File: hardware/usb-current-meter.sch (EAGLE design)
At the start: 30 parts, among them IC2 LM358, U1 ATTINY45, X1 MC2, X3 USB-A-H

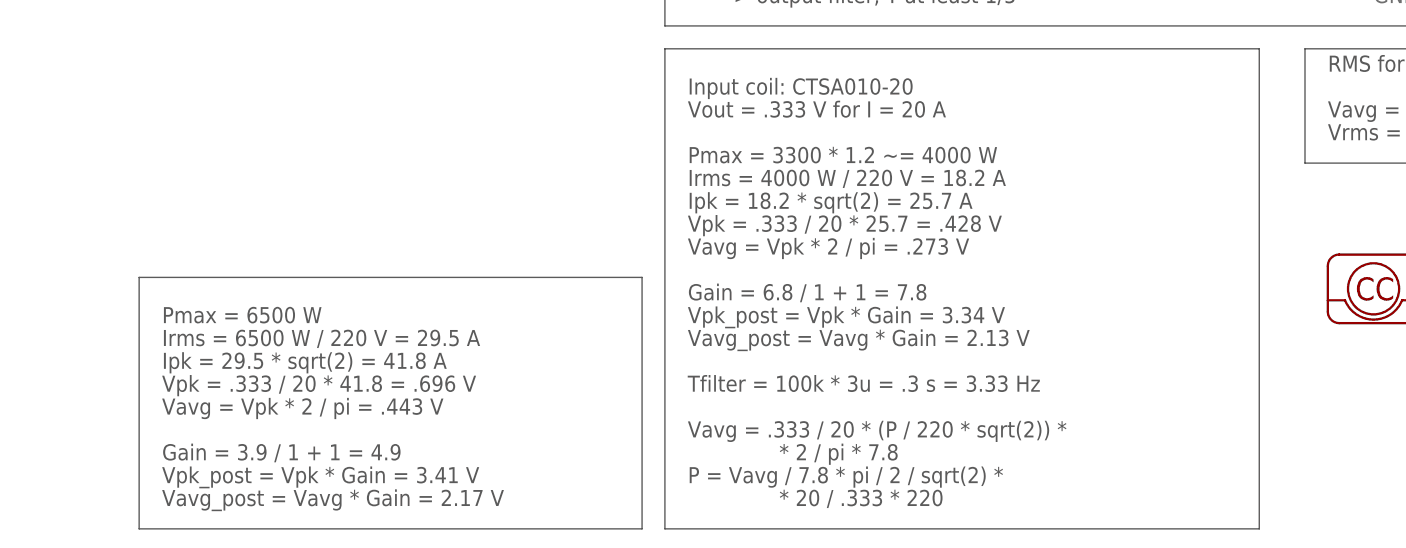
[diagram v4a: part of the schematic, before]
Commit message: hardware: re-made calculations for 230V (welcome to 2012)
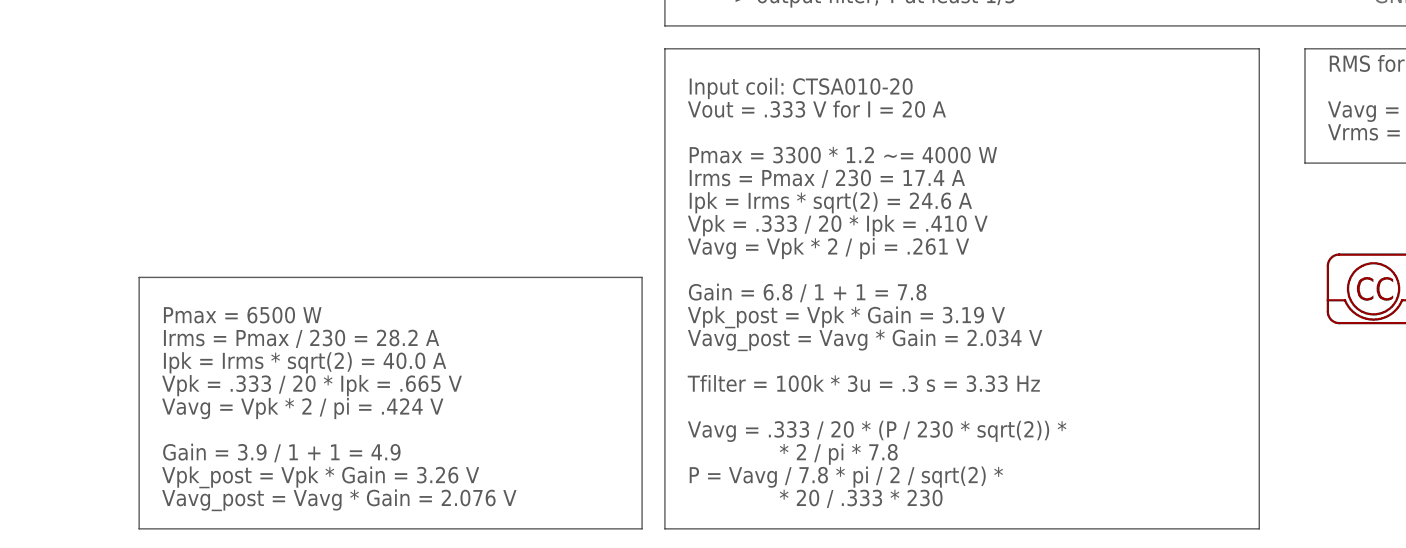
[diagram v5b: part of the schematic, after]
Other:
- note added: "* 20 / .333 * 230"
- note added: "Ipk = Irms * sqrt(2) = 24.6 A"
- note added: "Ipk = Irms * sqrt(2) = 40.0 A"
- note added: "Irms = Pmax / 230 = 17.4 A"
- note added: "Irms = Pmax / 230 = 28.2 A"
- note added: "Vavg = .333 / 20 * (P / 230 * sqrt(2)) *"
- note added: "Vavg = Vpk * 2 / pi = .261 V"
- note added: "Vavg = Vpk * 2 / pi = .424 V"
- note added: "Vavg_post = Vavg * Gain = 2.034 V"
- note added: "Vavg_post = Vavg * Gain = 2.076 V"
- note added: "Vpk = .333 / 20 * Ipk = .410 V"
- note added: "Vpk = .333 / 20 * Ipk = .665 V"
- note added: "Vpk_post = Vpk * Gain = 3.19 V"
- note added: "Vpk_post = Vpk * Gain = 3.26 V"
- note removed: "* 20 / .333 * 220"
- note removed: "Ipk = 18.2 * sqrt(2) = 25.7 A"
- note removed: "Ipk = 29.5 * sqrt(2) = 41.8 A"
- note removed: "Irms = 4000 W / 220 V = 18.2 A"
- note removed: "Irms = 6500 W / 220 V = 29.5 A"
- note removed: "Vavg = .333 / 20 * (P / 220 * sqrt(2)) *"
- note removed: "Vavg = Vpk * 2 / pi = .273 V"
- note removed: "Vavg = Vpk * 2 / pi = .443 V"
- note removed: "Vavg_post = Vavg * Gain = 2.13 V"
- note removed: "Vavg_post = Vavg * Gain = 2.17 V"
- note removed: "Vpk = .333 / 20 * 25.7 = .428 V"
- note removed: "Vpk = .333 / 20 * 41.8 = .696 V"
- note removed: "Vpk_post = Vpk * Gain = 3.34 V"
- note removed: "Vpk_post = Vpk * Gain = 3.41 V"
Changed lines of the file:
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@@
 <text x="99.06" y="60.96" size="1.778" layer="97">&gt; output filter, T at least 1/5</text>
 <text x="93.98" y="43.18" size="1.778" layer="97">Pmax = 3300 * 1.2 ~= 4000 W</text>
-<text x="93.98" y="40.64" size="1.778" layer="97">Irms = 4000 W / 220 V = 18.2 A</text>
-<text x="93.98" y="38.1" size="1.778" layer="97">Ipk = 18.2 * sqrt(2) = 25.7 A</text>
-<text x="93.98" y="35.56" size="1.778" layer="97">Vpk = .333 / 20 * 25.7 = .428 V</text>
+<text x="93.98" y="40.64" size="1.778" layer="97">Irms = Pmax / 230 = 17.4 A</text>
+<text x="93.98" y="38.1" size="1.778" layer="97">Ipk = Irms * sqrt(2) = 24.6 A</text>
+<text x="93.98" y="35.56" size="1.778" layer="97">Vpk = .333 / 20 * Ipk = .410 V</text>
 <text x="93.98" y="48.26" size="1.778" layer="97">Vout = .333 V for I = 20 A</text>
 <text x="93.98" y="50.8" size="1.778" layer="97">Input coil: CTSA010-20</text>
-<text x="93.98" y="33.02" size="1.778" layer="97">Vavg = Vpk * 2 / pi = .273 V</text>
+<text x="93.98" y="33.02" size="1.778" layer="97">Vavg = Vpk * 2 / pi = .261 V</text>
 <text x="93.98" y="27.94" size="1.778" layer="97">Gain = 6.8 / 1 + 1 = 7.8</text>
-<text x="93.98" y="25.4" size="1.778" layer="97">Vpk_post = Vpk * Gain = 3.34 V</text>
-<text x="93.98" y="22.86" size="1.778" layer="97">Vavg_post = Vavg * Gain = 2.13 V</text>
+<text x="93.98" y="25.4" size="1.778" layer="97">Vpk_post = Vpk * Gain = 3.19 V</text>
+<text x="93.98" y="22.86" size="1.778" layer="97">Vavg_post = Vavg * Gain = 2.034 V</text>
 <text x="165.1" y="53.34" size="1.778" layer="97">RMS for sine wave</text>
 <text x="165.1" y="48.26" size="1.778" layer="97">Vavg = Vpk * 2 / pi</text>
@@
 <wire x1="162.56" y1="43.18" x2="162.56" y2="55.88" width="0.1524" layer="97"/>
 <text x="93.98" y="17.78" size="1.778" layer="97">Tfilter = 100k * 3u = .3 s = 3.33 Hz</text>
-<text x="93.98" y="12.7" size="1.778" layer="97">Vavg = .333 / 20 * (P / 220 * sqrt(2)) *</text>
+<text x="93.98" y="12.7" size="1.778" layer="97">Vavg = .333 / 20 * (P / 230 * sqrt(2)) *</text>
 <text x="104.14" y="10.16" size="1.778" layer="97">* 2 / pi * 7.8</text>
 <text x="93.98" y="7.62" size="1.778" layer="97">P = Vavg / 7.8 * pi / 2 / sqrt(2) *</text>
-<text x="104.14" y="5.08" size="1.778" layer="97">* 20 / .333 * 220</text>
+<text x="104.14" y="5.08" size="1.778" layer="97">* 20 / .333 * 230</text>
 <text x="35.56" y="25.4" size="1.778" layer="97">Pmax = 6500 W</text>
-<text x="35.56" y="22.86" size="1.778" layer="97">Irms = 6500 W / 220 V = 29.5 A</text>
-<text x="35.56" y="20.32" size="1.778" layer="97">Ipk = 29.5 * sqrt(2) = 41.8 A</text>
-<text x="35.56" y="17.78" size="1.778" layer="97">Vpk = .333 / 20 * 41.8 = .696 V</text>
-<text x="35.56" y="15.24" size="1.778" layer="97">Vavg = Vpk * 2 / pi = .443 V</text>
+<text x="35.56" y="22.86" size="1.778" layer="97">Irms = Pmax / 230 = 28.2 A</text>
+<text x="35.56" y="20.32" size="1.778" layer="97">Ipk = Irms * sqrt(2) = 40.0 A</text>
+<text x="35.56" y="17.78" size="1.778" layer="97">Vpk = .333 / 20 * Ipk = .665 V</text>
+<text x="35.56" y="15.24" size="1.778" layer="97">Vavg = Vpk * 2 / pi = .424 V</text>
 <text x="35.56" y="10.16" size="1.778" layer="97">Gain = 3.9 / 1 + 1 = 4.9</text>
-<text x="35.56" y="7.62" size="1.778" layer="97">Vpk_post = Vpk * Gain = 3.41 V</text>
-<text x="35.56" y="5.08" size="1.778" layer="97">Vavg_post = Vavg * Gain = 2.17 V</text>
+<text x="35.56" y="7.62" size="1.778" layer="97">Vpk_post = Vpk * Gain = 3.26 V</text>
+<text x="35.56" y="5.08" size="1.778" layer="97">Vavg_post = Vavg * Gain = 2.076 V</text>
 <wire x1="33.02" y1="30.48" x2="88.9" y2="30.48" width="0.1524" layer="97"/>
 <wire x1="88.9" y1="30.48" x2="88.9" y2="2.54" width="0.1524" layer="97"/>

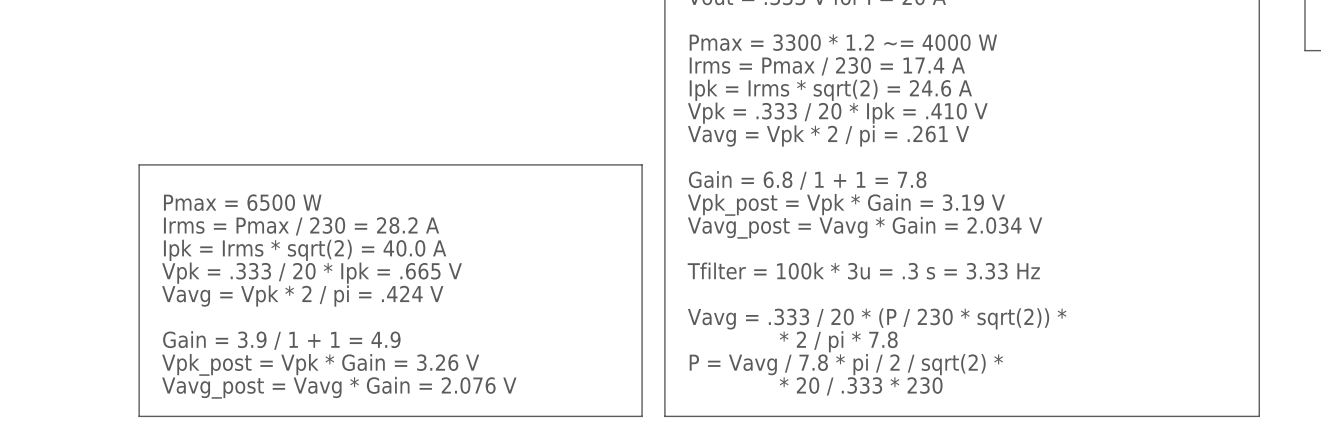
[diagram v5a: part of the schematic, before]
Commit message: hardware: change values for use with 1.1Vref
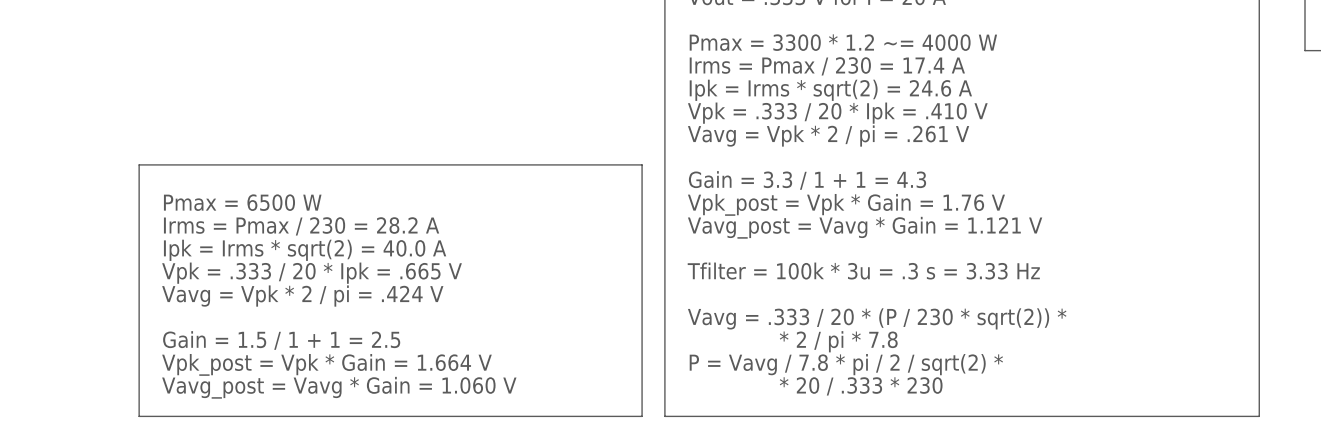
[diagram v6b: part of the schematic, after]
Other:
- note added: "Gain = 1.5 / 1 + 1 = 2.5"
- note added: "Gain = 3.3 / 1 + 1 = 4.3"
- note added: "Vavg_post = Vavg * Gain = 1.060 V"
- note added: "Vavg_post = Vavg * Gain = 1.121 V"
- note added: "Vpk_post = Vpk * Gain = 1.664 V"
- note added: "Vpk_post = Vpk * Gain = 1.76 V"
- note removed: "Gain = 3.9 / 1 + 1 = 4.9"
- note removed: "Gain = 6.8 / 1 + 1 = 7.8"
- note removed: "Vavg_post = Vavg * Gain = 2.034 V"
- note removed: "Vavg_post = Vavg * Gain = 2.076 V"
- note removed: "Vpk_post = Vpk * Gain = 3.19 V"
- note removed: "Vpk_post = Vpk * Gain = 3.26 V"
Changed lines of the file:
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@@
 <part name="R8" library="rcl" deviceset="R-EU_" device="R0603" value="tbd">
 <variant name="bias" populate="no"/>
-<variant name="rectifier" value="6.8k"/>
+<variant name="rectifier" value="3.3k"/>
 </part>
 <part name="GND8" library="supply1" deviceset="GND" device=""/>
@@
 <text x="93.98" y="50.8" size="1.778" layer="97">Input coil: CTSA010-20</text>
 <text x="93.98" y="33.02" size="1.778" layer="97">Vavg = Vpk * 2 / pi = .261 V</text>
-<text x="93.98" y="27.94" size="1.778" layer="97">Gain = 6.8 / 1 + 1 = 7.8</text>
-<text x="93.98" y="25.4" size="1.778" layer="97">Vpk_post = Vpk * Gain = 3.19 V</text>
-<text x="93.98" y="22.86" size="1.778" layer="97">Vavg_post = Vavg * Gain = 2.034 V</text>
+<text x="93.98" y="27.94" size="1.778" layer="97">Gain = 3.3 / 1 + 1 = 4.3</text>
+<text x="93.98" y="25.4" size="1.778" layer="97">Vpk_post = Vpk * Gain = 1.76 V</text>
+<text x="93.98" y="22.86" size="1.778" layer="97">Vavg_post = Vavg * Gain = 1.121 V</text>
 <text x="165.1" y="53.34" size="1.778" layer="97">RMS for sine wave</text>
 <text x="165.1" y="48.26" size="1.778" layer="97">Vavg = Vpk * 2 / pi</text>
@@
 <text x="35.56" y="17.78" size="1.778" layer="97">Vpk = .333 / 20 * Ipk = .665 V</text>
 <text x="35.56" y="15.24" size="1.778" layer="97">Vavg = Vpk * 2 / pi = .424 V</text>
-<text x="35.56" y="10.16" size="1.778" layer="97">Gain = 3.9 / 1 + 1 = 4.9</text>
-<text x="35.56" y="7.62" size="1.778" layer="97">Vpk_post = Vpk * Gain = 3.26 V</text>
-<text x="35.56" y="5.08" size="1.778" layer="97">Vavg_post = Vavg * Gain = 2.076 V</text>
+<text x="35.56" y="10.16" size="1.778" layer="97">Gain = 1.5 / 1 + 1 = 2.5</text>
+<text x="35.56" y="7.62" size="1.778" layer="97">Vpk_post = Vpk * Gain = 1.664 V</text>
+<text x="35.56" y="5.08" size="1.778" layer="97">Vavg_post = Vavg * Gain = 1.060 V</text>
 <wire x1="33.02" y1="30.48" x2="88.9" y2="30.48" width="0.1524" layer="97"/>
 <wire x1="88.9" y1="30.48" x2="88.9" y2="2.54" width="0.1524" layer="97"/>

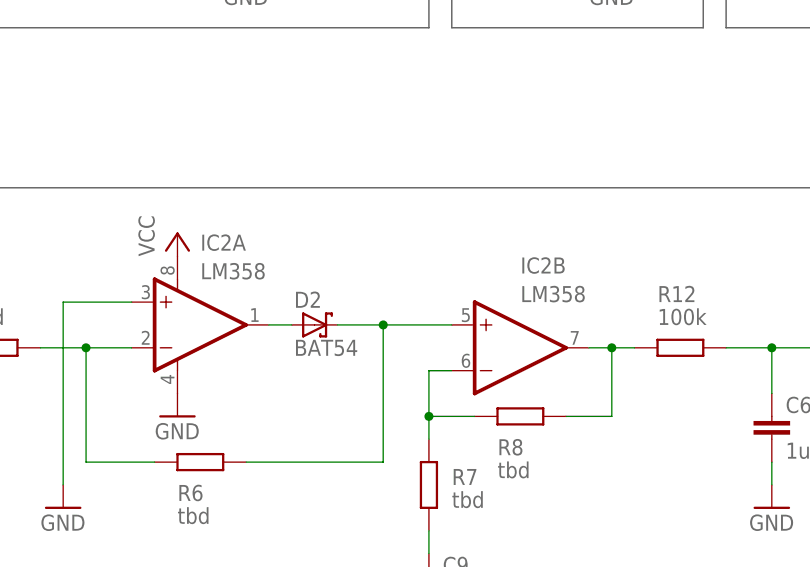
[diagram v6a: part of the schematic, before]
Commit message: hw: change opamp to lt2078
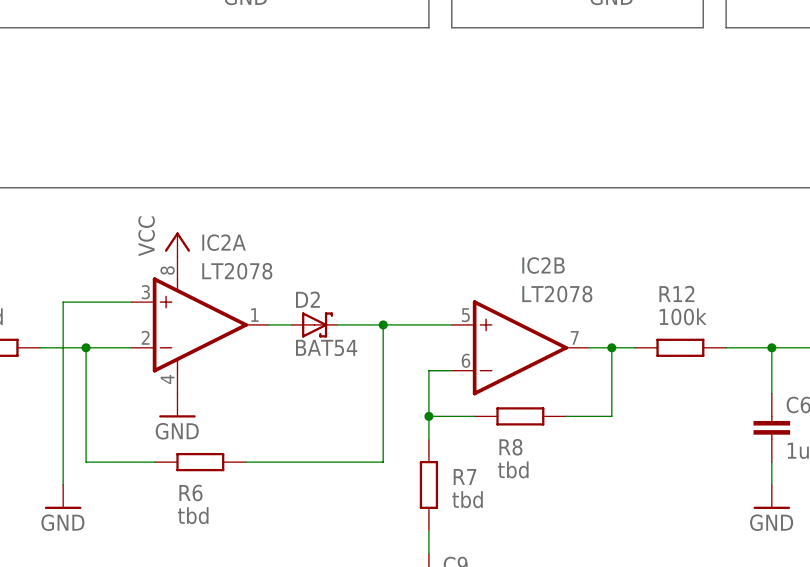
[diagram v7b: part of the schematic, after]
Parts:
- IC2: value LM358 -> LT2078
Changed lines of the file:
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@@
 <?xml version="1.0" encoding="utf-8"?>
 <!DOCTYPE eagle SYSTEM "eagle.dtd">
-<eagle version="6.1">
+<eagle version="6.2">
 <drawing>
 <settings>
@@
 <part name="R1" library="rcl" deviceset="R-EU_" device="R0603" value="68"/>
 <part name="X3" library="SparkFun" deviceset="USB" device="-A-H"/>
-<part name="IC2" library="burr-brown" deviceset="OPA2234" device="U" value="LM358">
+<part name="IC2" library="burr-brown" deviceset="OPA2234" device="U" value="LT2078">
 <variant name="bias" populate="no" value="OPA2234U"/>
 </part>

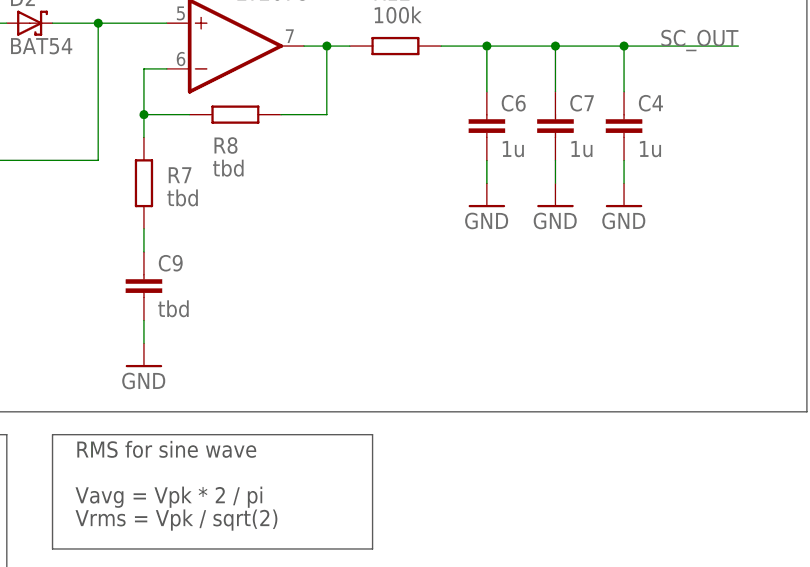
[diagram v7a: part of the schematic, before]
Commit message: hw: add note about series-cap
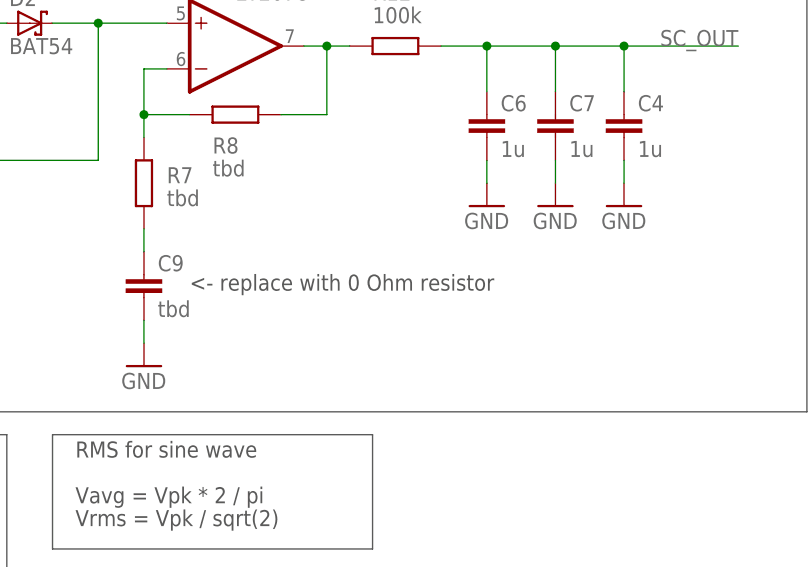
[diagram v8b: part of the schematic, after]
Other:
- note added: "<- replace with 0 Ohm resistor"
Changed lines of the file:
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@@
 <?xml version="1.0" encoding="utf-8"?>
 <!DOCTYPE eagle SYSTEM "eagle.dtd">
-<eagle version="6.2">
+<eagle version="6.3">
 <drawing>
 <settings>
@@
 <wire x1="88.9" y1="2.54" x2="33.02" y2="2.54" width="0.1524" layer="97"/>
 <wire x1="33.02" y1="2.54" x2="33.02" y2="30.48" width="0.1524" layer="97"/>
+<text x="177.8" y="73.66" size="1.778" layer="97" rot="MR180">&lt;- replace with 0 Ohm resistor</text>
 </plain>
 <instances>
